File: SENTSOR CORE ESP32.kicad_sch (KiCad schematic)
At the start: 84 parts, among them J1 HYC80-TF08-375, J2 Conn_01x10_Pin, J3 Conn_01x10_Pin, J4 Conn_01x10_Pin, J5 JST_PH 2.0mm, J6 TYPEC-304S-ACP16, Q1 SL8205S, Q2 CJ2301, Q3 UMH3N, SW1 SW_Push, SW2 SW_Push, U1 ESP32-WROOM-32UE, U2 DS3231MZ, U3 XC6220B331MR, U4 XC6220B331MR, U5 BQ27441DRZR-G1B, U6 CN3165, U7 DW01A, U8 USBLC6-2SC6, U9 CH340K

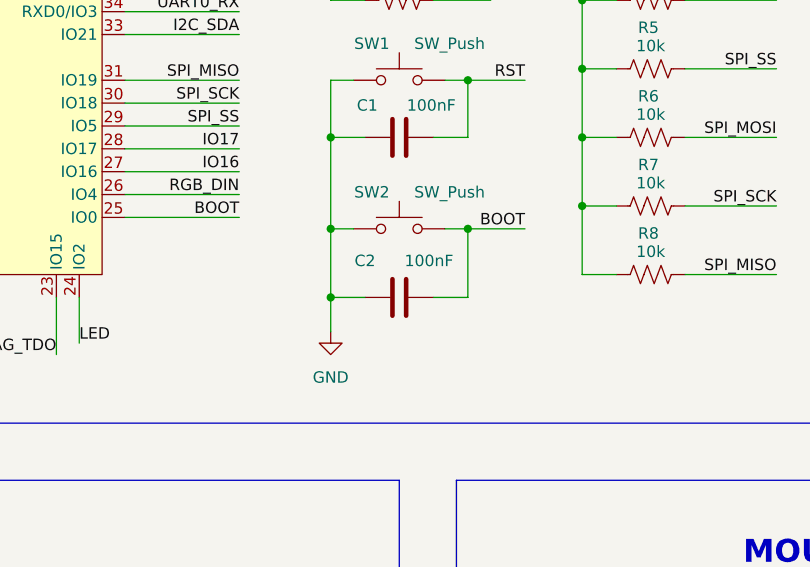
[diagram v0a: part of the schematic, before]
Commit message: add board cut line
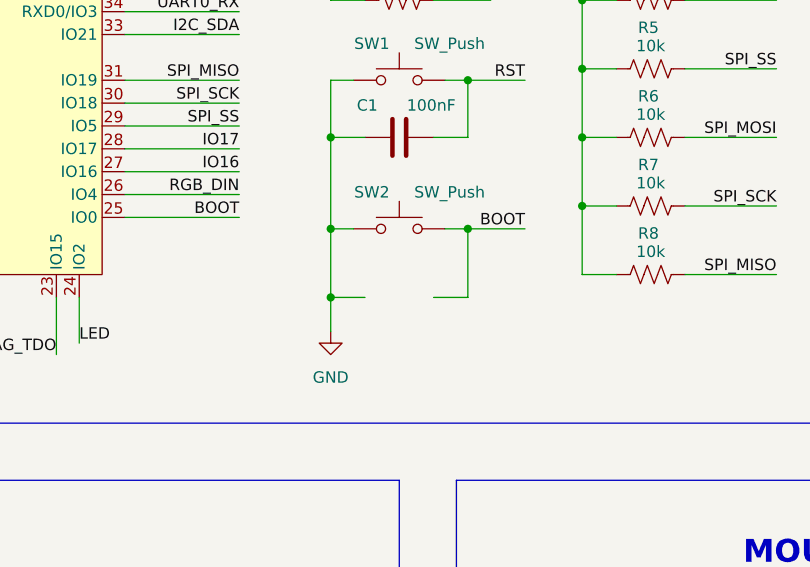
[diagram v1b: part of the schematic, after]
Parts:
- removed C2: 100nF, Capacitor_SMD:C_0402_1005Metric_Pad0.74x0.62mm_HandSolder, symbol Device:C
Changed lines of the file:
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@@
-	)
-	(symbol
-		(lib_id "Device:C")
-		(at 292.1 201.93 90)
-		(unit 1)
-		(exclude_from_sim no)
-		(in_bom yes)
-		(on_board yes)
-		(dnp no)
-		(property "Reference" "C2"
-			(at 288.29 197.866 90)
-			(effects
-				(font
-					(size 1.27 1.27)
-				)
-			)
-		)
-		(property "Value" "100nF"
-			(at 295.402 197.866 90)
-			(effects
-				(font
-					(size 1.27 1.27)
-				)
-			)
-		)
-		(property "Footprint" "Capacitor_SMD:C_0402_1005Metric_Pad0.74x0.62mm_HandSolder"
-			(at 295.91 200.9648 0)
-			(effects
-				(font
-					(size 1.27 1.27)
-				)
-				(hide yes)
-			)
-		)
-		(property "Datasheet" "~"
-			(at 292.1 201.93 0)
-			(effects
-				(font
-					(size 1.27 1.27)
-				)
-				(hide yes)
-			)
-		)
-		(property "Description" "Unpolarized capacitor"
-			(at 292.1 201.93 0)
-			(effects
-				(font
-					(size 1.27 1.27)
-				)
-				(hide yes)
-			)
-		)
-		(pin "1"
-		)
-		(pin "2"
-		)
-		(instances
-			(project "SENTSOR CORE ESP32"
-				(path "/5e6dd74d-2c01-41ea-aa13-bdd7206128e8"
-					(reference "C2")
-					(unit 1)
-				)
-			)
-		)
 	)
 	(symbol

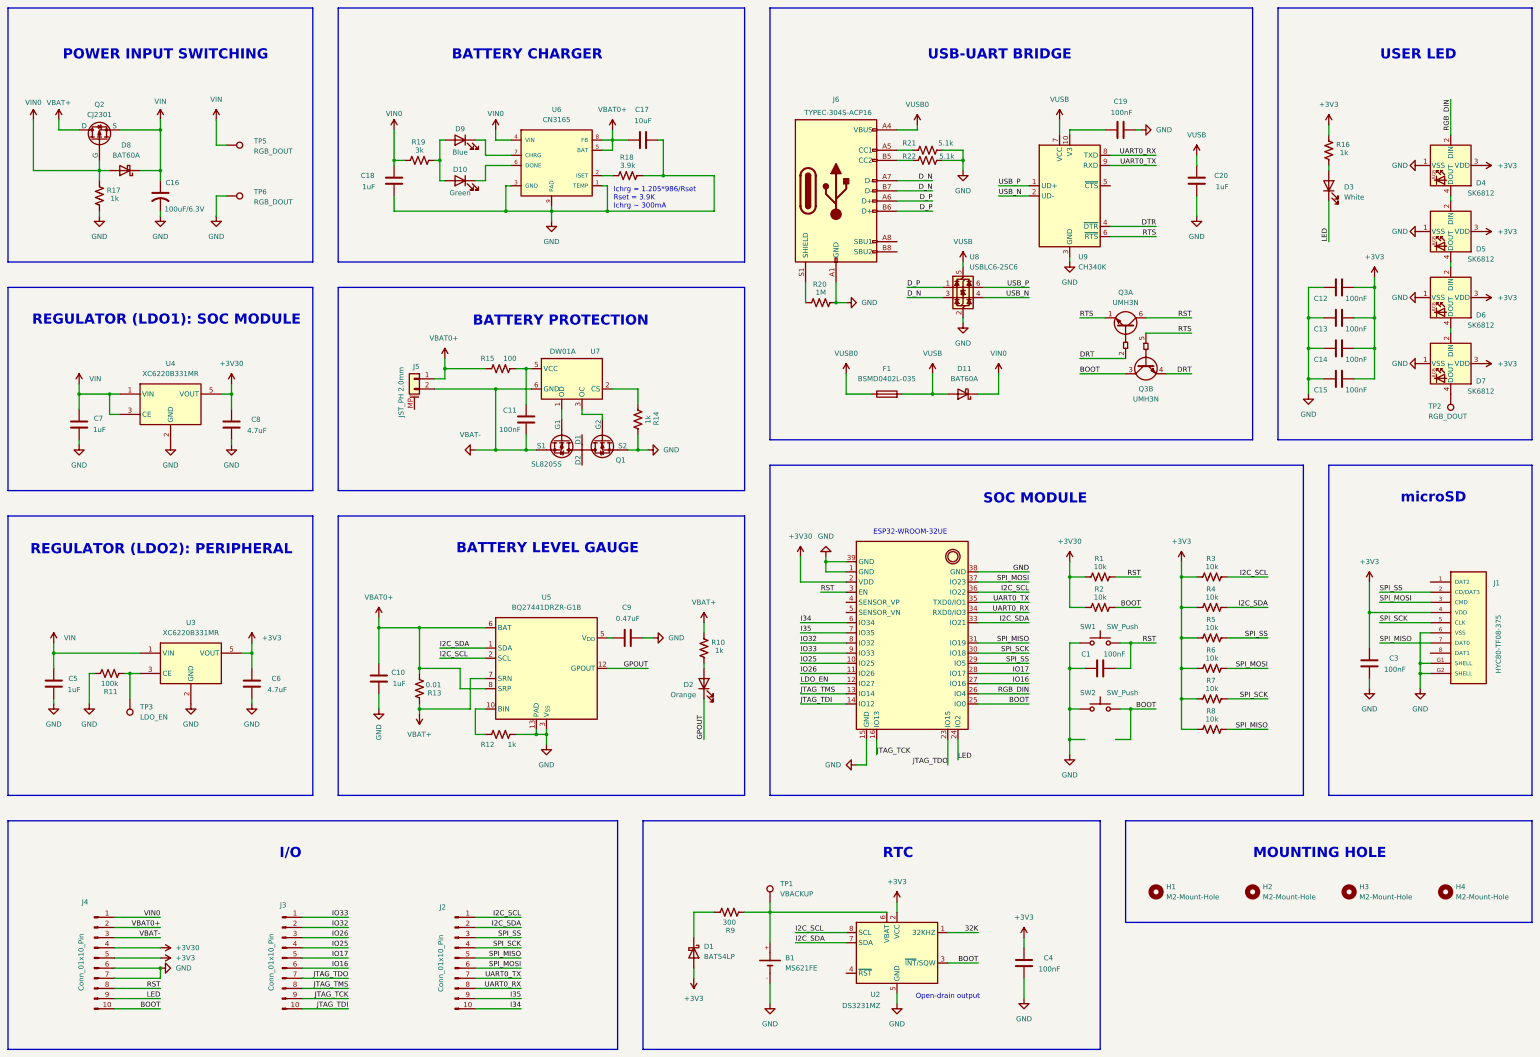
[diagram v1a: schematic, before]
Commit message: add board layout
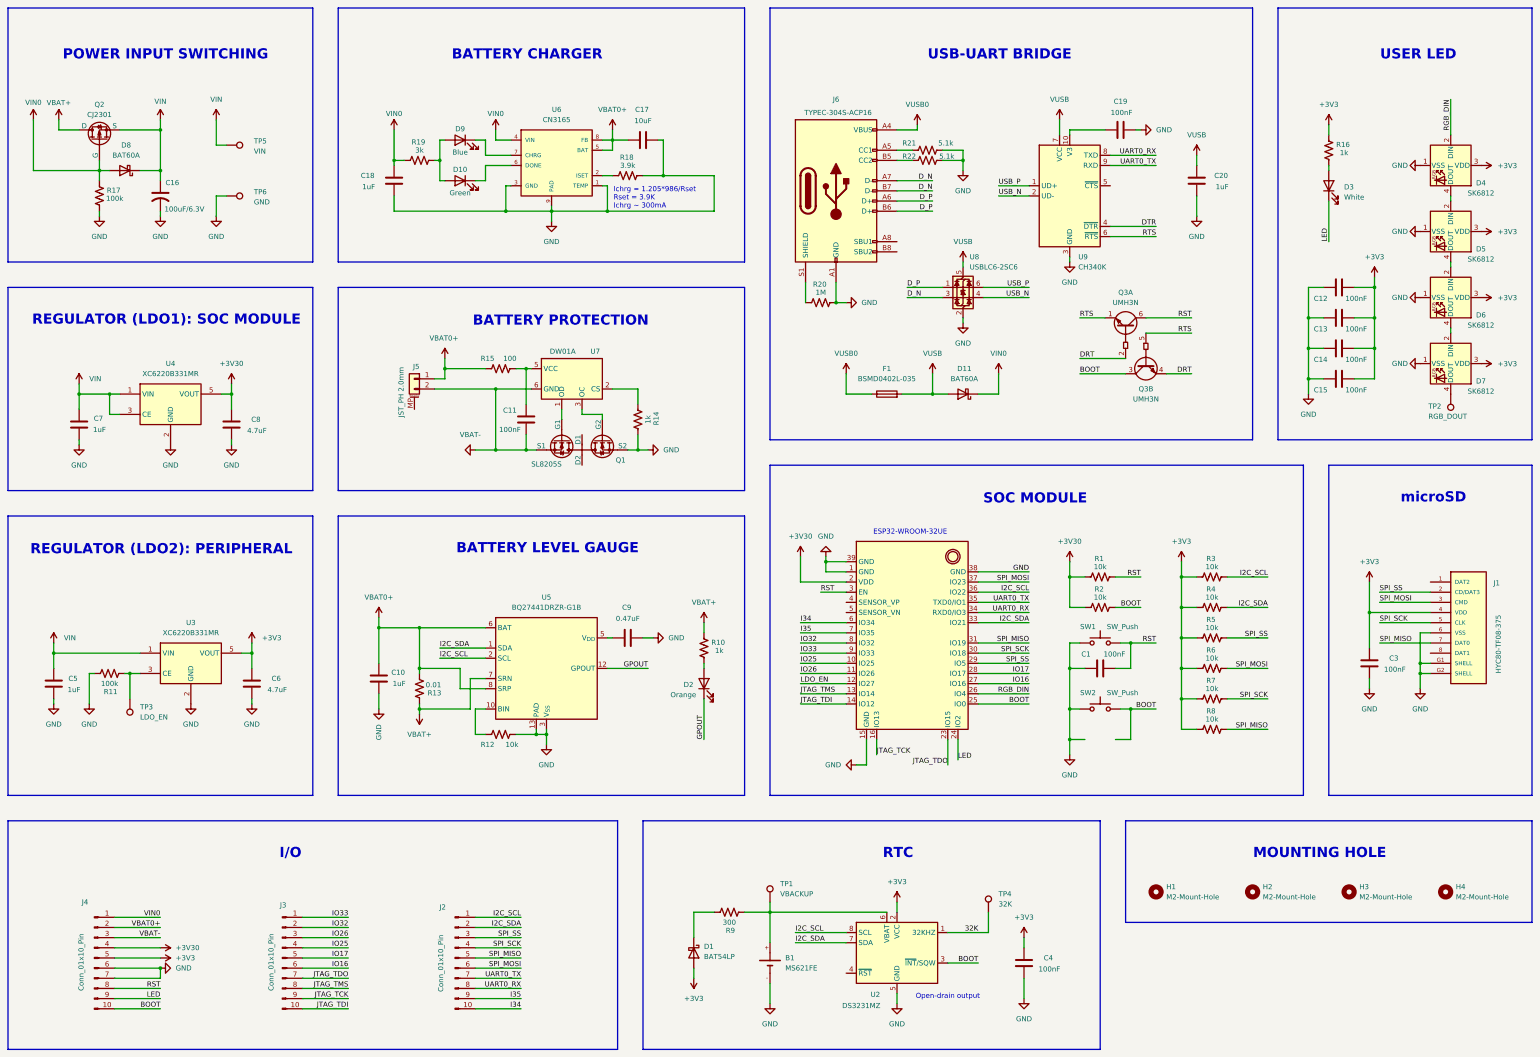
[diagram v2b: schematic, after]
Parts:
- added TP4: 32K, lib:TestPoint_Pad_D0.7mm, symbol Connector:TestPoint
- C17: footprint Capacitor_SMD:C_0402_1005Metric_Pad0.74x0.62mm_HandSolder -> Capacitor_SMD:C_0603_1608Metric
- R12: value 1k -> 10k
- R17: value 1k -> 100k
- R18, R20: footprint Resistor_SMD:R_0402_1005Metric_Pad0.72x0.64mm_HandSolder -> Resistor_SMD:R_0603_1608Metric
- TP1: footprint Connector_Pin:Pin_D0.7mm_L6.5mm_W1.8mm_FlatFork -> lib:TestPoint_Pad_D0.7mm
- TP2, TP3: footprint Connector_Pin:Pin_D0.7mm_L6.5mm_W1.8mm_FlatFork -> TestPoint_Pad_D0.7mm
- TP5: value RGB_DOUT -> VIN; footprint Connector_Pin:Pin_D0.7mm_L6.5mm_W1.8mm_FlatFork -> TestPoint_Pad_D0.7mm
- TP6: value RGB_DOUT -> GND; footprint Connector_Pin:Pin_D0.7mm_L6.5mm_W1.8mm_FlatFork -> TestPoint_Pad_D0.7mm
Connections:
- net 32K: now also TP4.1
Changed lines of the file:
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@@
 	(wire
 		(pts
+			(xy 264.16 245.11) (xy 264.16 250.19)
+		)
+		(stroke
+			(width 0)
+			(type default)
+		)
+	)
+	(wire
+		(pts
 			(xy 135.89 62.23) (xy 138.43 62.23)
 		)
@@
 	(wire
 		(pts
-			(xy 254 250.19) (xy 261.62 250.19)
+			(xy 254 250.19) (xy 264.16 250.19)
 		)
 		(stroke
@@
 			)
 		)
-		(property "Value" "RGB_DOUT"
+		(property "Value" "GND"
 			(at 80.518 67.564 90)
 			(effects
@@
 			)
 		)
-		(property "Footprint" "Connector_Pin:Pin_D0.7mm_L6.5mm_W1.8mm_FlatFork"
+		(property "Footprint" "TestPoint_Pad_D0.7mm"
 			(at 73.66 71.12 0)
 			(effects
@@
 			)
 		)
-		(property "Footprint" "Capacitor_SMD:C_0402_1005Metric_Pad0.74x0.62mm_HandSolder"
+		(property "Footprint" "Capacitor_SMD:C_0603_1608Metric"
 			(at 173.99 53.0352 0)
 			(effects
@@
 			)
 		)
-		(property "Footprint" "Connector_Pin:Pin_D0.7mm_L6.5mm_W1.8mm_FlatFork"
+		(property "Footprint" "TestPoint_Pad_D0.7mm"
 			(at 44.45 191.77 0)
 			(effects
@@
 	)
 	(symbol
+		(lib_id "Connector:TestPoint")
+		(at 264.16 245.11 0)
+		(unit 1)
+		(exclude_from_sim no)
+		(in_bom yes)
+		(on_board yes)
+		(dnp no)
+		(fields_autoplaced yes)
+		(property "Reference" "TP4"
+			(at 266.7 240.5379 0)
+			(effects
+				(font
+					(size 1.27 1.27)
+				)
+				(justify left)
+			)
+		)
+		(property "Value" "32K"
+			(at 266.7 243.0779 0)
+			(effects
+				(font
+					(size 1.27 1.27)
+				)
+				(justify left)
+			)
+		)
+		(property "Footprint" "lib:TestPoint_Pad_D0.7mm"
+			(at 269.24 245.11 0)
+			(effects
+				(font
+					(size 1.27 1.27)
+				)
+				(hide yes)
+			)
+		)
+		(property "Datasheet" "~"
+			(at 269.24 245.11 0)
+			(effects
+				(font
+					(size 1.27 1.27)
+				)
+				(hide yes)
+			)
+		)
+		(property "Description" "test point"
+			(at 264.16 245.11 0)
+			(effects
+				(font
+					(size 1.27 1.27)
+				)
+				(hide yes)
+			)
+		)
+		(pin "1"
+		)
+		(instances
+			(project "SENTSOR CORE ESP32"
+				(path "/5e6dd74d-2c01-41ea-aa13-bdd7206128e8"
+					(reference "TP4")
+					(unit 1)
+				)
+			)
+		)
+	)
+	(symbol
 		(lib_id "power:GND")
 		(at 372.11 91.44 270)
@@
 			)
 		)
-		(property "Value" "1k"
+		(property "Value" "10k"
 			(at 145.034 203.2 90)
 			(effects
@@
 			)
 		)
-		(property "Footprint" "Resistor_SMD:R_0402_1005Metric_Pad0.72x0.64mm_HandSolder"
+		(property "Footprint" "Resistor_SMD:R_0603_1608Metric"
 			(at 222.504 91.694 90)
 			(effects
@@
 			)
 		)
-		(property "Value" "RGB_DOUT"
+		(property "Value" "VIN"
 			(at 80.518 54.864 90)
 			(effects
@@
 			)
 		)
-		(property "Footprint" "Connector_Pin:Pin_D0.7mm_L6.5mm_W1.8mm_FlatFork"
+		(property "Footprint" "TestPoint_Pad_D0.7mm"
 			(at 73.66 58.42 0)
 			(effects
@@
 			)
 		)
-		(property "Footprint" "Connector_Pin:Pin_D0.7mm_L6.5mm_W1.8mm_FlatFork"
+		(property "Footprint" "TestPoint_Pad_D0.7mm"
 			(at 374.65 115.57 0)
 			(effects
@@
 			)
 		)
-		(property "Footprint" "Connector_Pin:Pin_D0.7mm_L6.5mm_W1.8mm_FlatFork"
+		(property "Footprint" "lib:TestPoint_Pad_D0.7mm"
 			(at 214.63 242.57 0)
 			(effects
@@
 			)
 		)
-		(property "Value" "1k"
+		(property "Value" "100k"
 			(at 45.72 66.675 0)
 			(effects
@@
 			)
 		)
-		(property "Footprint" "Resistor_SMD:R_0402_1005Metric_Pad0.72x0.64mm_HandSolder"
+		(property "Footprint" "Resistor_SMD:R_0603_1608Metric"
 			(at 174.244 59.944 90)
 			(effects

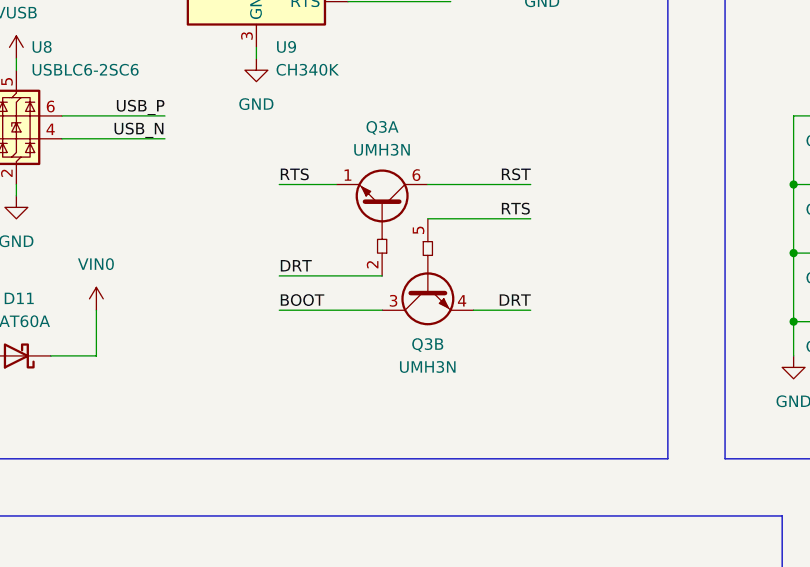
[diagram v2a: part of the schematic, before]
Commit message: add board layout
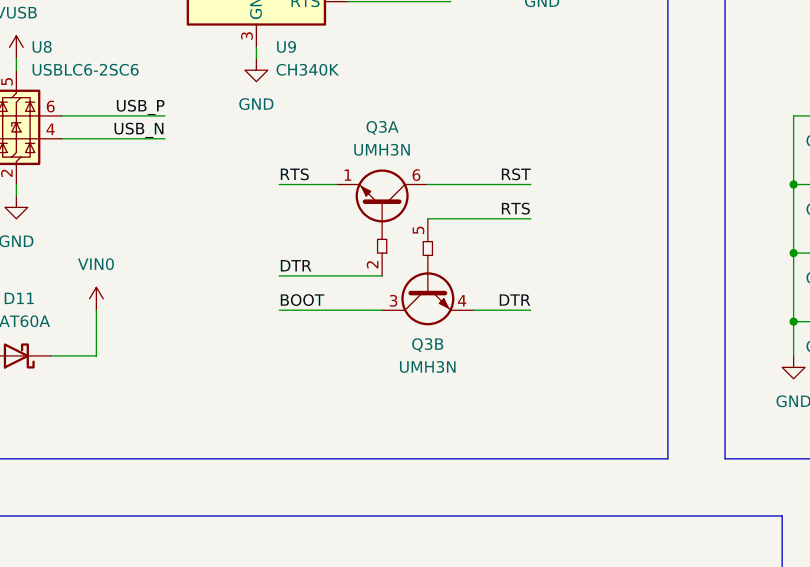
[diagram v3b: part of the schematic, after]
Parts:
- C18, C4: footprint Capacitor_SMD:C_0402_1005Metric_Pad0.74x0.62mm_HandSolder -> Capacitor_SMD:C_0402_1005Metric
- D1: footprint Diode_SMD:D_0603_1608Metric_Pad1.05x0.95mm_HandSolder -> Diode_SMD:D_0402_1005Metric_Pad0.77x0.64mm_HandSolder
- R12: footprint Resistor_SMD:R_0402_1005Metric_Pad0.72x0.64mm_HandSolder -> Resistor_SMD:R_0402_1005Metric
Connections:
- net DRT is gone; now on net DTR: Q3.2 (B1), Q3.4 (E2)
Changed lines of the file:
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@@
 		)
 	)
-	(label "DRT"
+	(label "DTR"
 		(at 287.02 106.68 0)
 		(effects
@@
 		)
 	)
-	(label "DRT"
+	(label "DTR"
 		(at 314.96 110.49 180)
 		(effects
@@
 			)
 		)
-		(property "Footprint" "Resistor_SMD:R_0402_1005Metric_Pad0.72x0.64mm_HandSolder"
+		(property "Footprint" "Resistor_SMD:R_0402_1005Metric"
 			(at 141.986 201.676 90)
 			(effects
@@
 			)
 		)
-		(property "Footprint" "Capacitor_SMD:C_0402_1005Metric_Pad0.74x0.62mm_HandSolder"
+		(property "Footprint" "Capacitor_SMD:C_0402_1005Metric"
 			(at 272.0848 254 0)
 			(effects
@@
 			)
 		)
-		(property "Footprint" "Capacitor_SMD:C_0402_1005Metric_Pad0.74x0.62mm_HandSolder"
+		(property "Footprint" "Capacitor_SMD:C_0402_1005Metric"
 			(at 116.5352 66.04 0)
 			(effects
@@
 			)
 		)
-		(property "Footprint" "Diode_SMD:D_0603_1608Metric_Pad1.05x0.95mm_HandSolder"
+		(property "Footprint" "Diode_SMD:D_0402_1005Metric_Pad0.77x0.64mm_HandSolder"
 			(at 190.5 255.27 0)
 			(effects

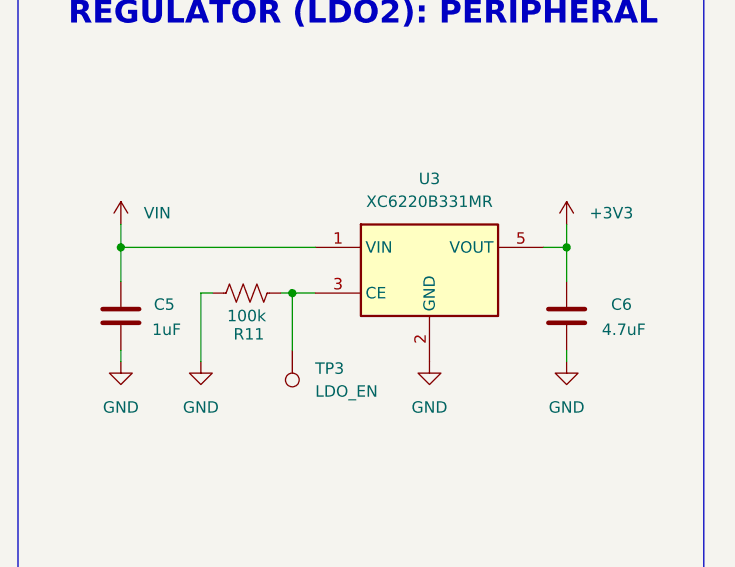
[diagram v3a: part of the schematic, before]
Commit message: add board layout 85%
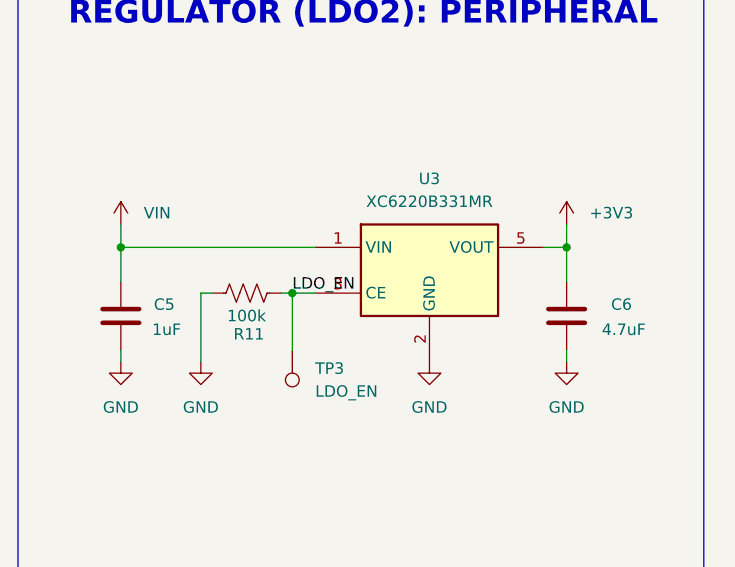
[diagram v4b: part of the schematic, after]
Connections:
- net LDO_EN: now also R11.1, TP3.1, U3.3 (CE)
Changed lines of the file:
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@@
+		)
+	)
+	(label "LDO_EN"
+		(at 49.53 185.42 0)
+		(effects
+			(font
+				(size 1.27 1.27)
+			)
+			(justify left bottom)
 		)
 	)
